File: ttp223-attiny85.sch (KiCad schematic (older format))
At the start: 10 parts, among them Q1 PN2222A, Q2 Nch Power MOSFET, U1 TL431LP, U2 ATtiny85-20PU

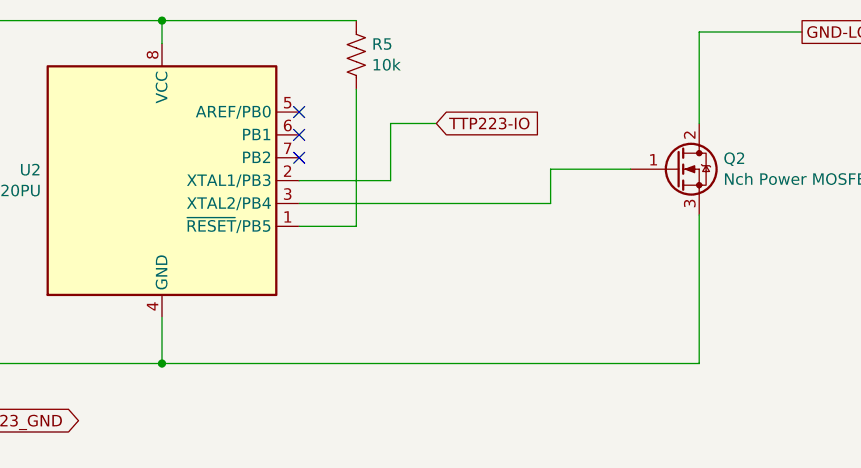
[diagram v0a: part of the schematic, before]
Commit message: Add resistor for preventing hi-z power on.
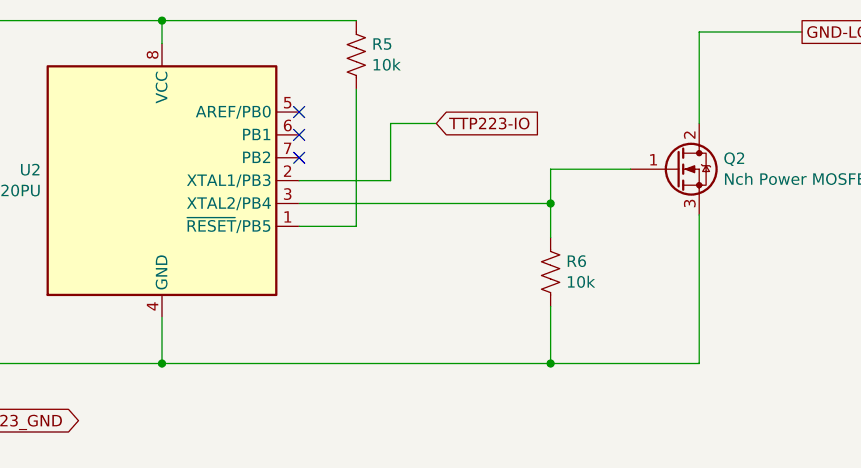
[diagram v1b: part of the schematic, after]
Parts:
- added R6: 10k, symbol Device:R_US
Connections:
- net GND: now also R6.2
- net at Q2.1 (G), U2.3 (XTAL2/PB4): now also R6.1
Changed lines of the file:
@@
 EESchema Schematic File Version 4
+LIBS:ttp223-attiny85-cache
 EELAYER 30 0
 EELAYER END
@@
 	6800 2850 7150 2850
 Wire Wire Line
-	5100 3700 7450 3700
+	5100 3700 6800 3700
 Wire Wire Line
 	7450 3700 7450 3050
@@
 Text Notes 1450 2800 0    50   ~ 0
 Remove @ VCC>15V
+$Comp
+L Device:R_US R6
+U 1 1 5DBED0FC
+P 6800 3300
+F 0 "R6" H 6868 3346 50  0000 L CNN
+F 1 "10k" H 6868 3255 50  0000 L CNN
+F 2 "" V 6840 3290 50  0001 C CNN
+F 3 "~" H 6800 3300 50  0001 C CNN
+	1    6800 3300
+	1    0    0    -1
+$EndComp
+Wire Wire Line
+	6800 3450 6800 3700
+Connection ~ 6800 3700
+Wire Wire Line
+	6800 3700 7450 3700
+Wire Wire Line
+	6800 3150 6800 3000
+Connection ~ 6800 3000
 $EndSCHEMATC

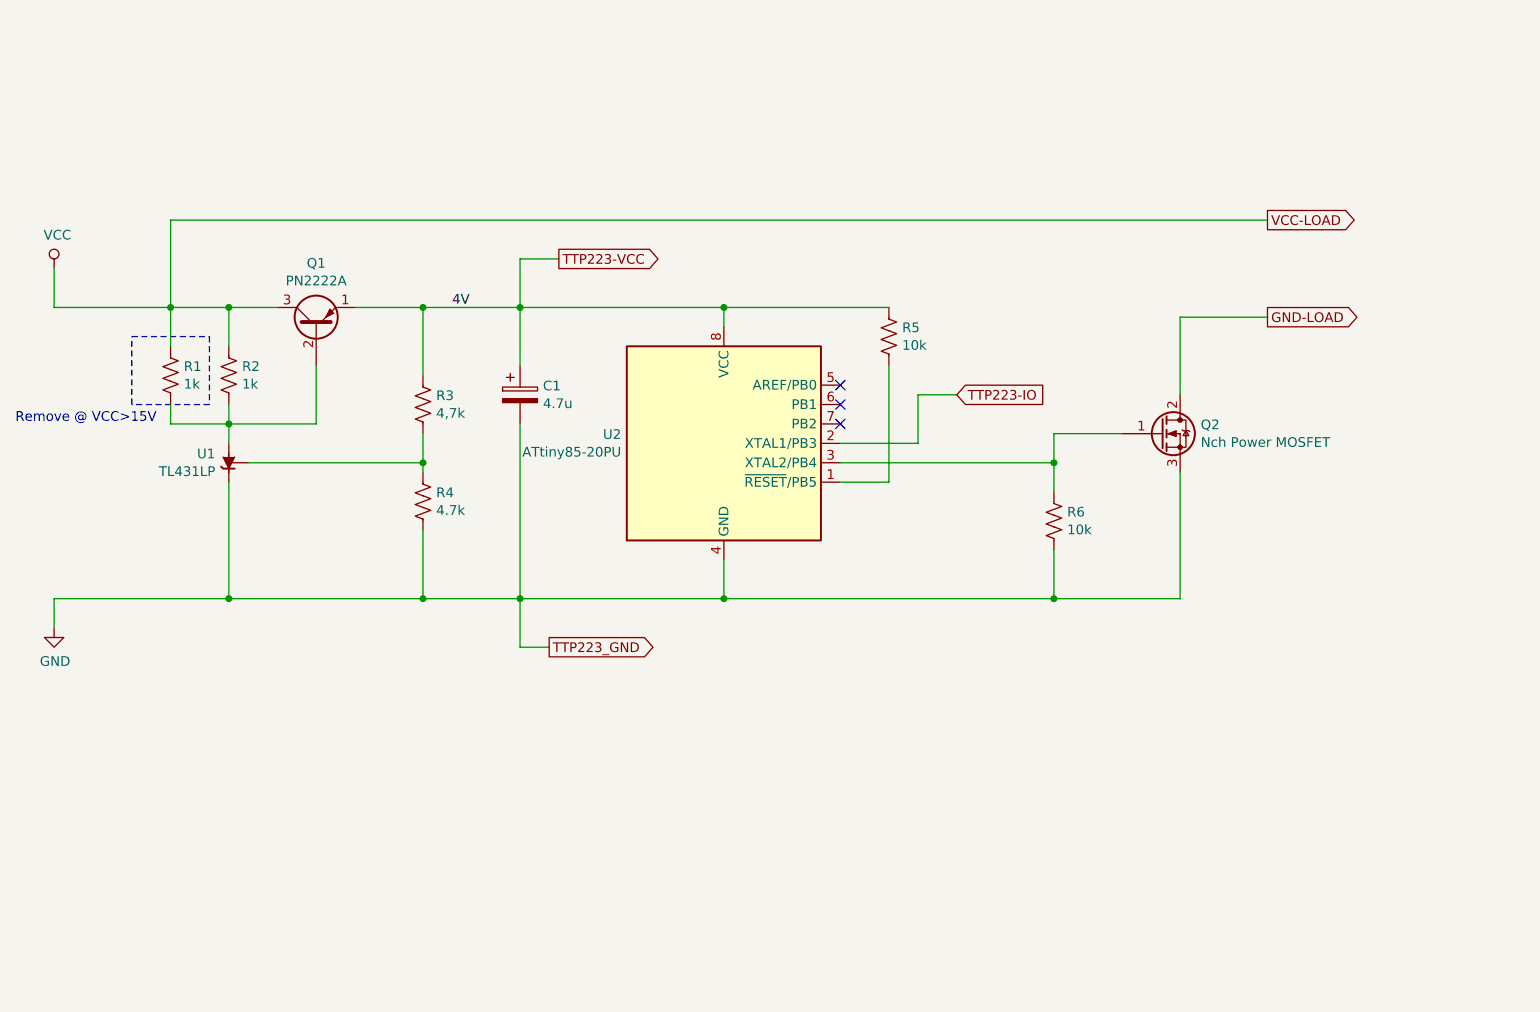
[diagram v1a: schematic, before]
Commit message: Using 12F675 instead of ATTiny85. Selectable.
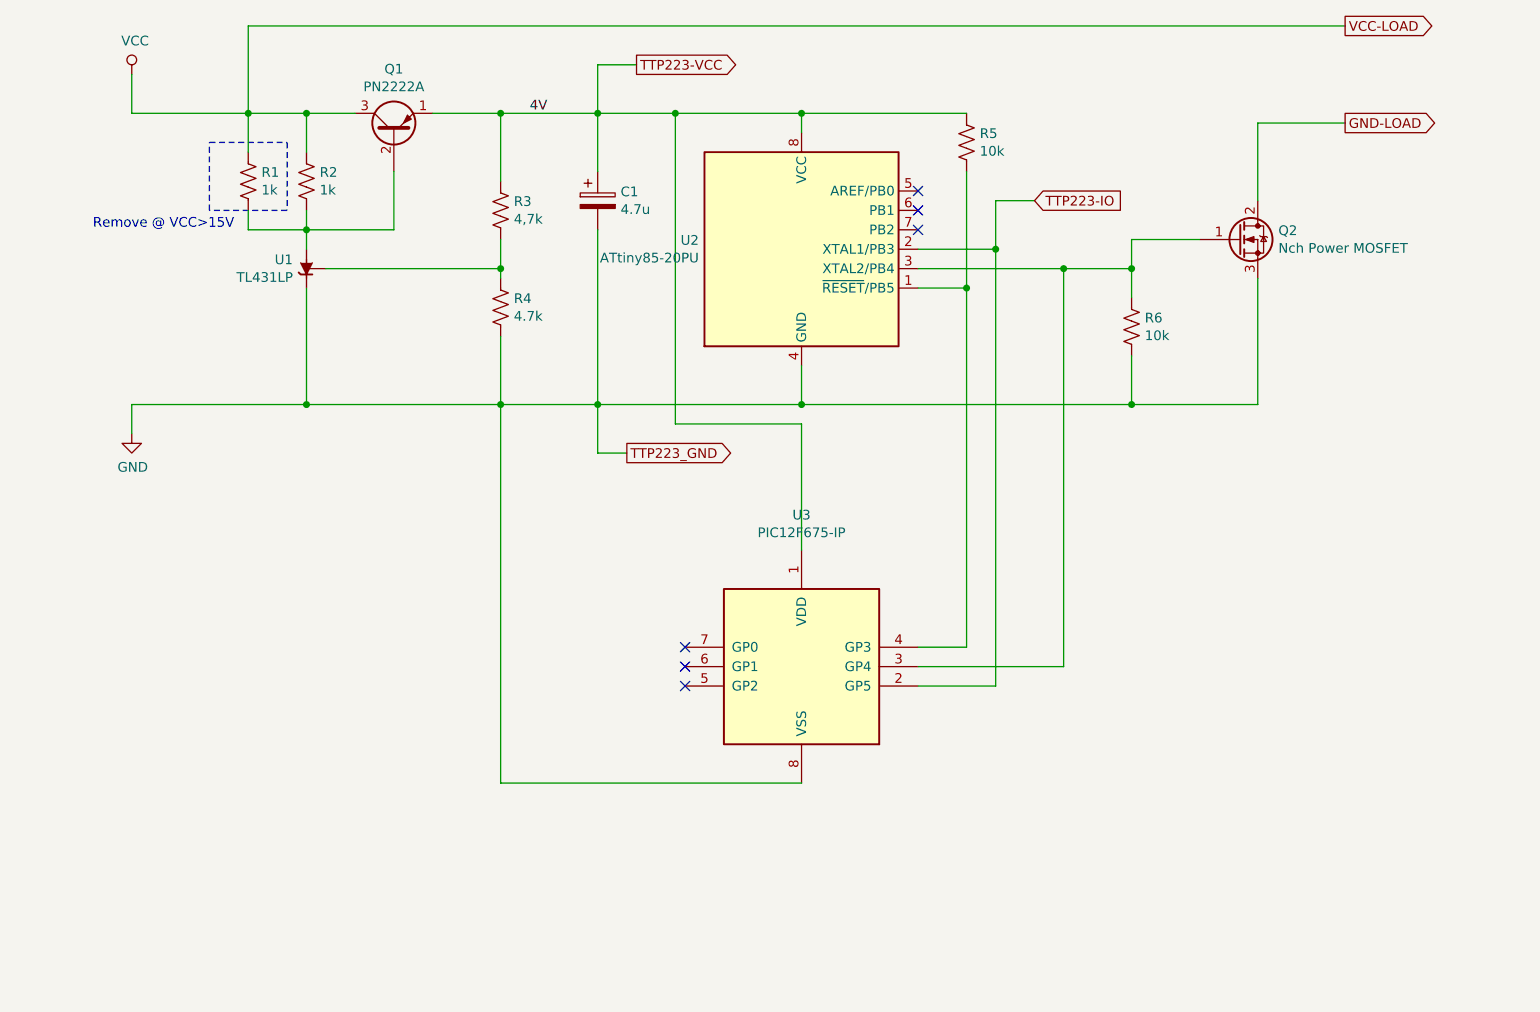
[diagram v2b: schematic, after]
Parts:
- added U3: PIC12F675-IP, Package_DIP:DIP-8_W7.62mm, symbol MCU_Microchip_PIC12:PIC12F675-IP
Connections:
- net GND: now also U3.8 (VSS)
- net TTP223-IO: now also U3.2 (GP5)
- net TTP223-VCC: now also U3.1 (VDD)
- net at R5.2, U2.1 (~RESET~/PB5): now also U3.4 (GP3)
- net at Q2.1 (G), R6.1, U2.3 (XTAL2/PB4): now also U3.3 (GP4)
- no-connect marks 3 -> 6
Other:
- moved on the sheet: C1, Q1, Q2, R1, R2, R3, R4, R5, R6, U1, U2

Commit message: Add box.
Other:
- note added: "12F675"
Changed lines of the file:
@@
 Wire Wire Line
 	4850 1200 5500 1200
+Wire Notes Line
+	3800 3150 7100 3150
+Wire Notes Line
+	7100 3150 7100 4750
+Wire Notes Line
+	7100 4750 3800 4750
+Wire Notes Line
+	3800 4750 3800 3150
+Text Notes 4100 3150 0    50   ~ 0
+12F675
 $EndSCHEMATC

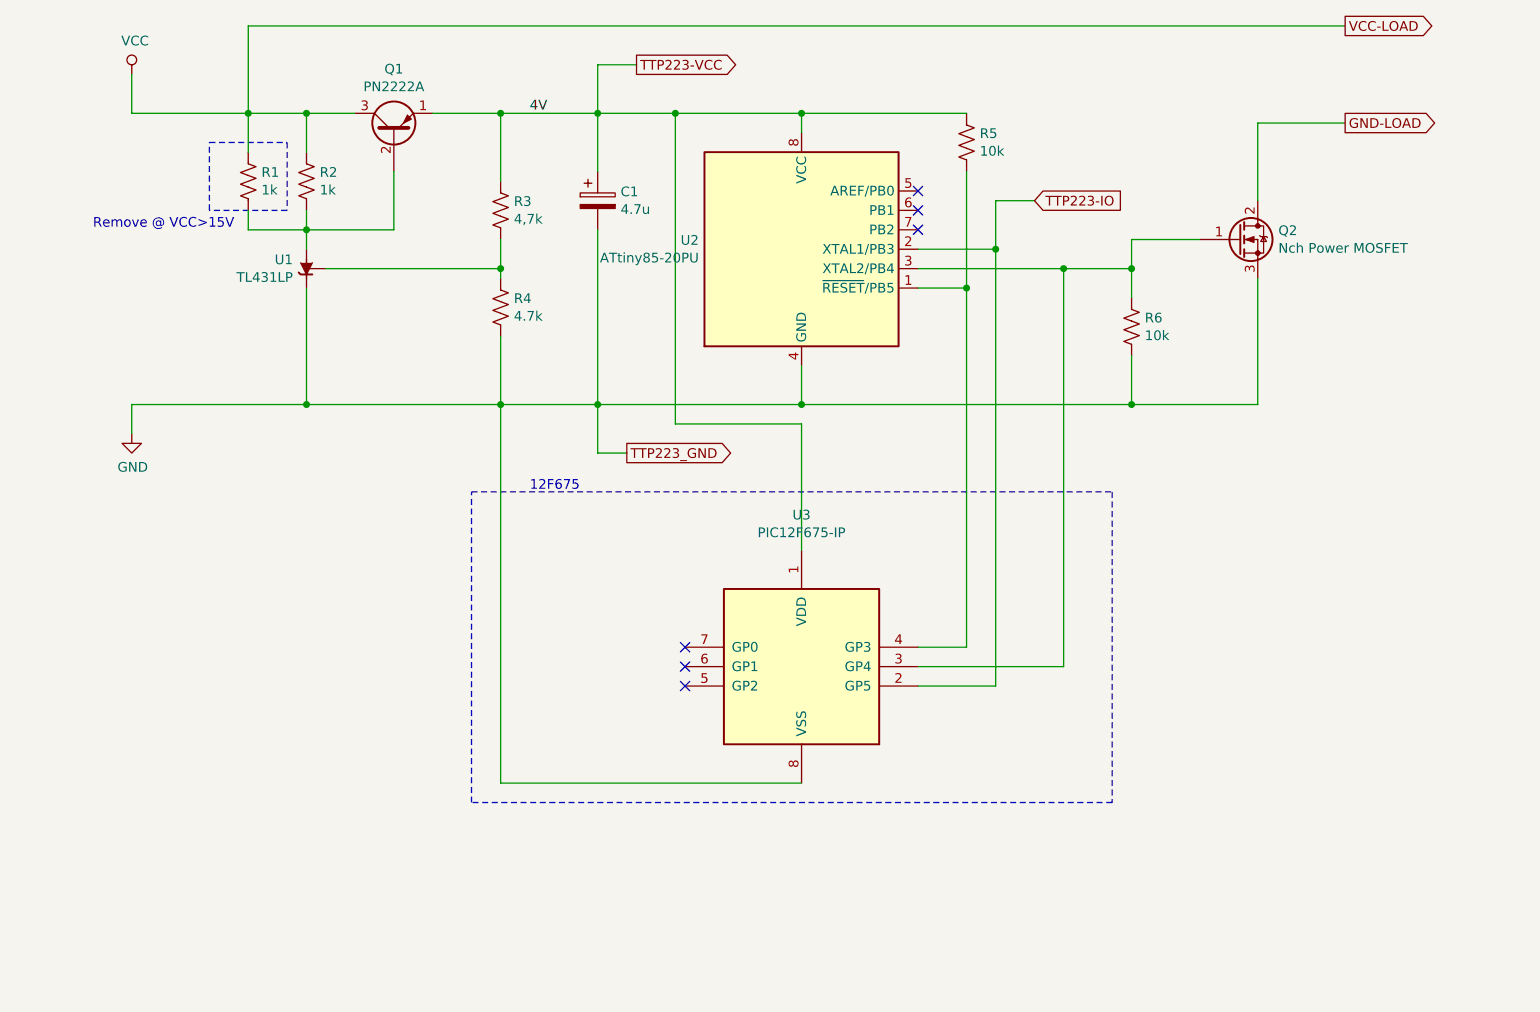
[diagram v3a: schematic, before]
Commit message: Fix TL431 power regulation.
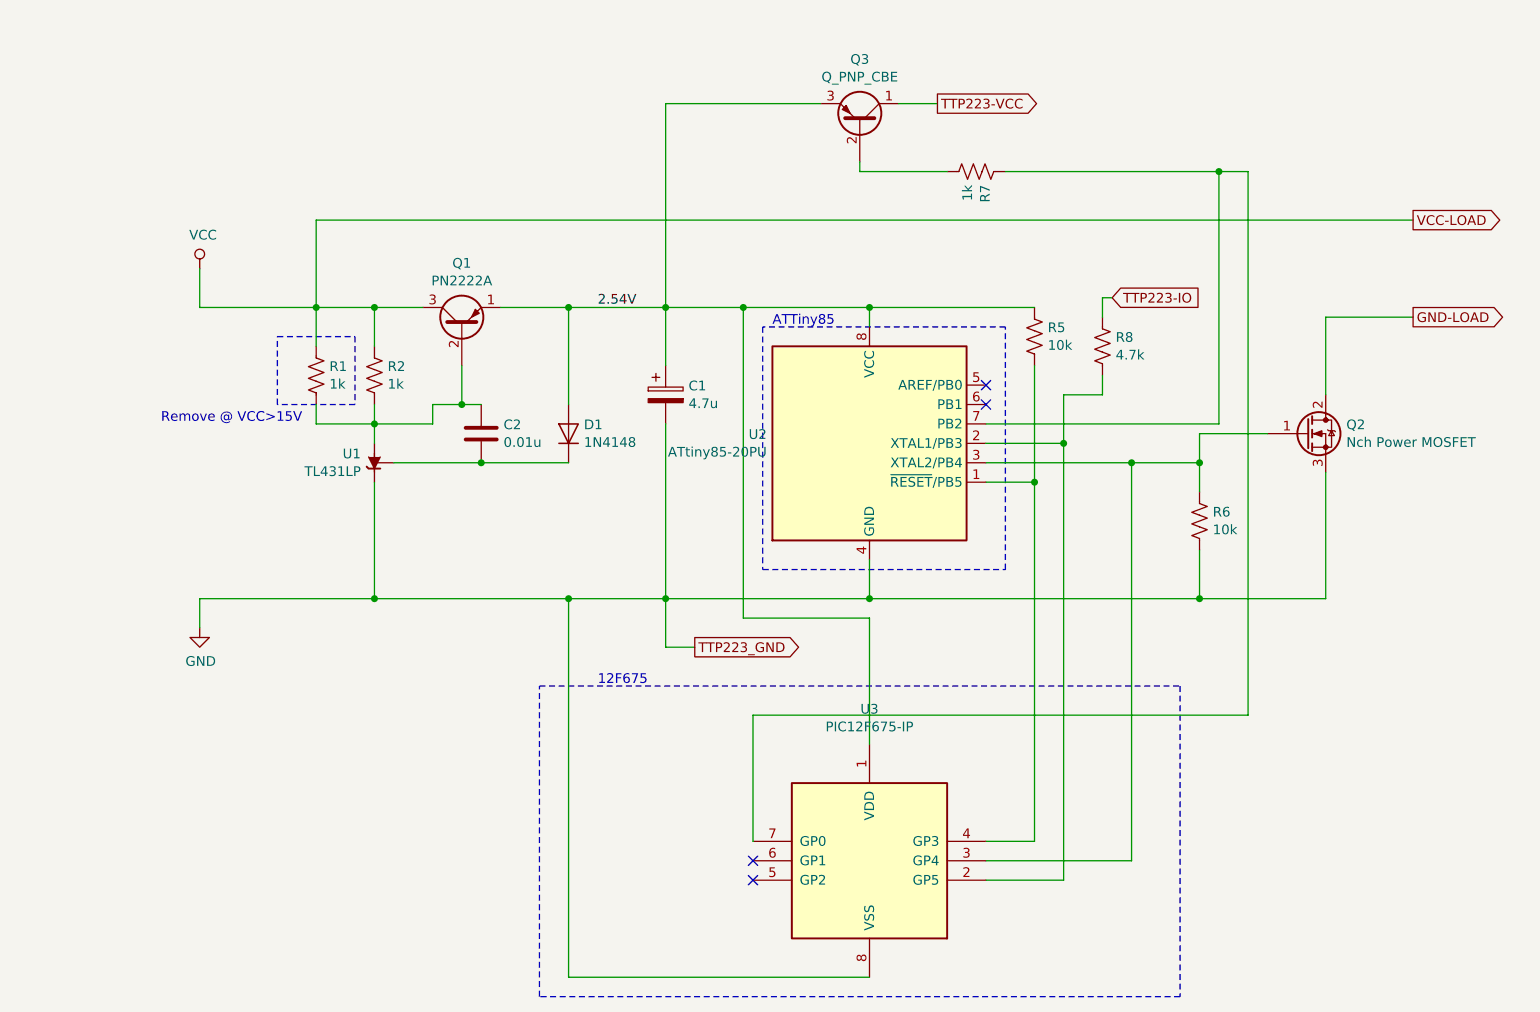
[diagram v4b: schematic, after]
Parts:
- removed R3: 4,7k, symbol Device:R_US
- removed R4: 4.7k, symbol Device:R_US
- added C2: 0.01u, symbol Device:C
- added D1: 1N4148, Diode_THT:D_DO-35_SOD27_P7.62mm_Horizontal, symbol Diode:1N4148
- added Q3: Q_PNP_CBE, symbol Device:Q_PNP_CBE
- added R7: 1k, symbol Device:R_US
- added R8: 4.7k, symbol Device:R_US
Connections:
- net TTP223-IO: now also R8.1; no longer U2.2 (XTAL1/PB3), U3.2 (GP5)
- net TTP223-VCC: now also Q3.1 (C); no longer C1.1, Q1.1 (E), R5.1, U2.8 (VCC), U3.1 (VDD)
- net at U2.7 (PB2): now also U3.7 (GP0), R7.1
- net at U1.1 (REF): now also C2.2, D1.1 (K)
- net at Q1.2 (B), R1.2, R2.2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: now also C2.1
- new net: R8.2, U2.2 (XTAL1/PB3), U3.2 (GP5)
- new net: Q3.2 (B), R7.2
- new net 2.54V: C1.1, D1.2 (A), Q1.1 (E), Q3.3 (E), R5.1, U2.8 (VCC), U3.1 (VDD)
- no-connect marks 6 -> 4
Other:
- note added: "ATTiny85"
- moved on the sheet: C1, Q1, Q2, R1, R2, R5, R6, U1, U2, U3

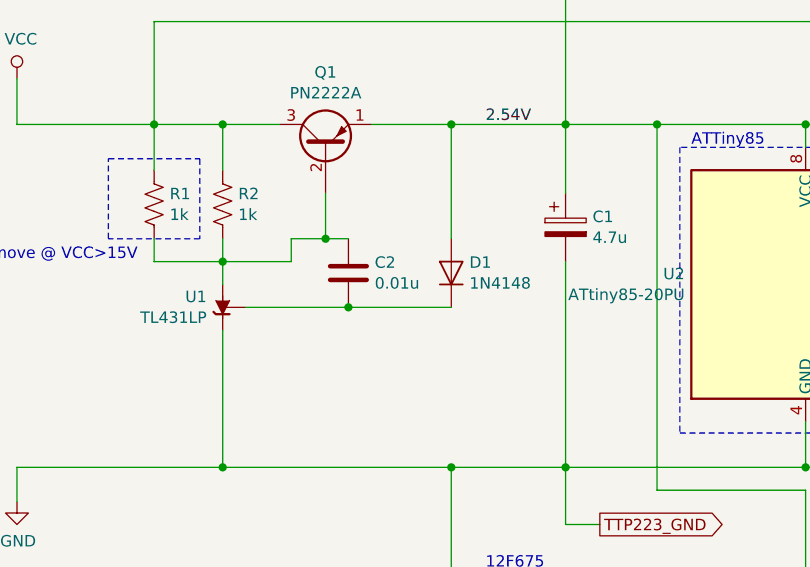
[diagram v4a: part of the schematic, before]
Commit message: Change capacitor to 0.1uF
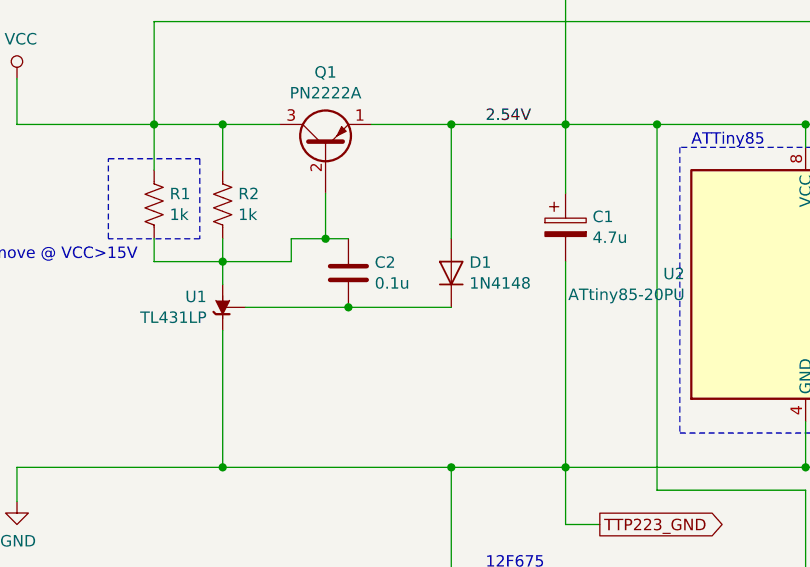
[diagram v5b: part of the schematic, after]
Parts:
- C2: value 0.01u -> 0.1u
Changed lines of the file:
@@
 P 3850 2850
 F 0 "C2" H 3965 2896 50  0000 L CNN
-F 1 "0.01u" H 3965 2805 50  0000 L CNN
+F 1 "0.1u" H 3965 2805 50  0000 L CNN
 F 2 "" H 3888 2700 50  0001 C CNN
 F 3 "~" H 3850 2850 50  0001 C CNN

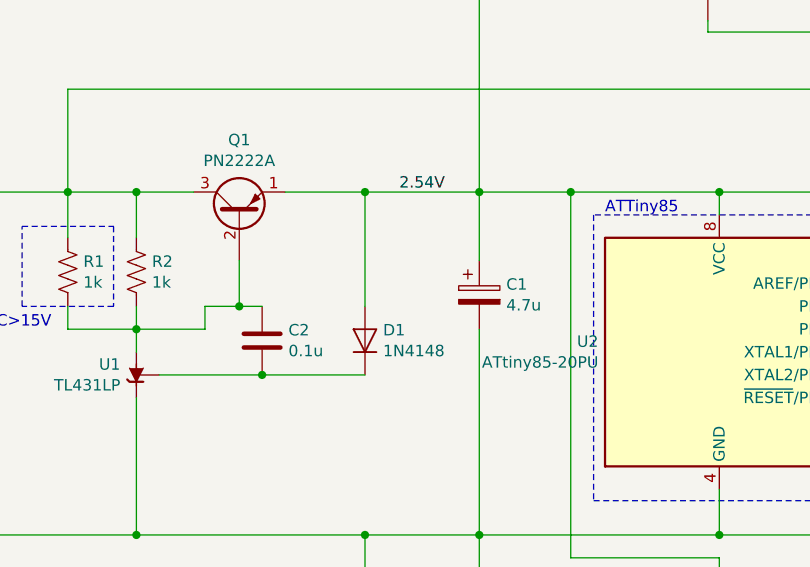
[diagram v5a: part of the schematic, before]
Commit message: Remove diode.
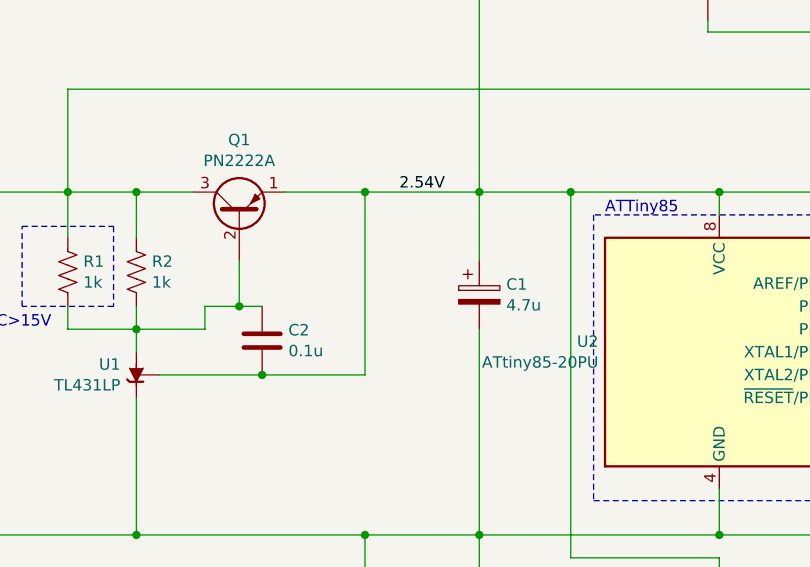
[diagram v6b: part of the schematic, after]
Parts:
- removed D1: 1N4148, Diode_THT:D_DO-35_SOD27_P7.62mm_Horizontal, symbol Diode:1N4148
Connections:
- net 2.54V: now also C2.2, U1.1 (REF)
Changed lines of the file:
@@
 Wire Wire Line
 	3950 2200 4300 2200
-$Comp
-L Diode:1N4148 D1
-U 1 1 5E0C7315
-P 4300 2850
-F 0 "D1" V 4346 2771 50  0000 R CNN
-F 1 "1N4148" V 4255 2771 50  0000 R CNN
-F 2 "Diode_THT:D_DO-35_SOD27_P7.62mm_Horizontal" H 4300 2675 50  0001 C CNN
-F 3 "https://assets.nexperia.com/documents/data-sheet/1N4148_1N4448.pdf" H 4300 2850 50  0001 C CNN
-	1    4300 2850
-	0    -1   -1   0
-$EndComp
-Wire Wire Line
-	4300 2700 4300 2200
 Connection ~ 4300 2200
 Wire Wire Line
@@
 	3600 2700 3750 2700
 Connection ~ 3750 2700
+Wire Wire Line
+	4300 2200 4300 3000
 $EndSCHEMATC
